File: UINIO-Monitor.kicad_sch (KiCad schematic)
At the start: 38 parts, among them J1 Conn_01x09_Male, J2 Conn_01x09_Male, J3 Conn_01x04_Male, P1 LCD_Pad_10Pin, P2 LCD_Pad_12Pin, P3 OLED_Pad_30Pin, U1 ME6211, U2 ME6211, U3 XC6206PxxxMR

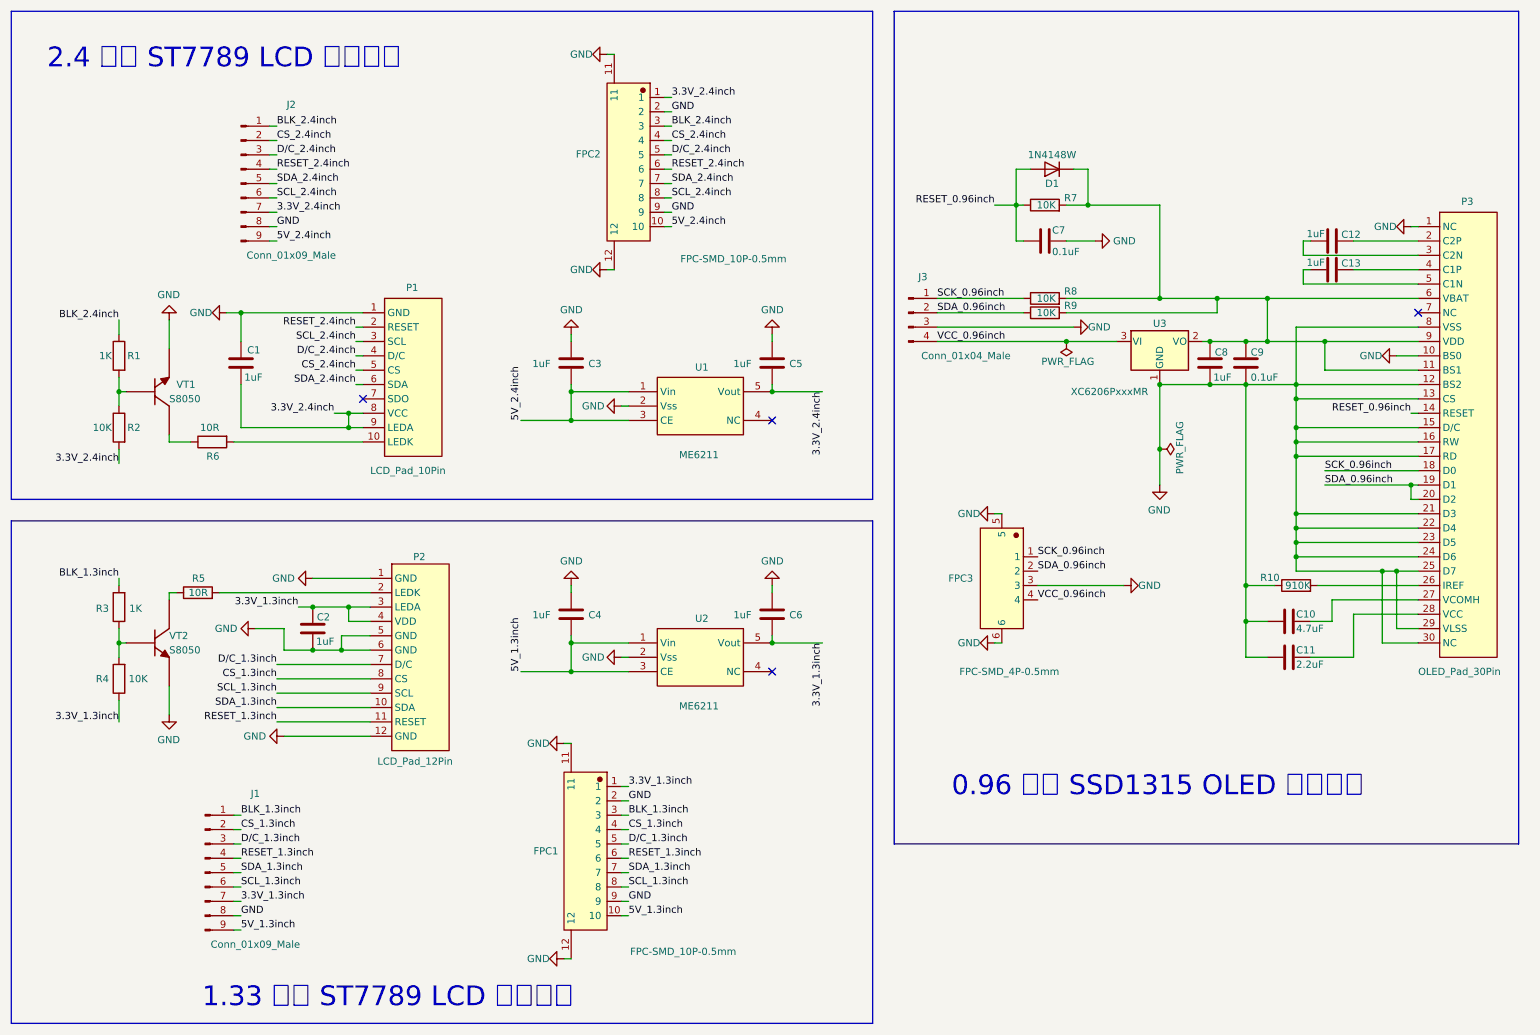
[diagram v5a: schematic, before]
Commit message: Complete PCB routing.
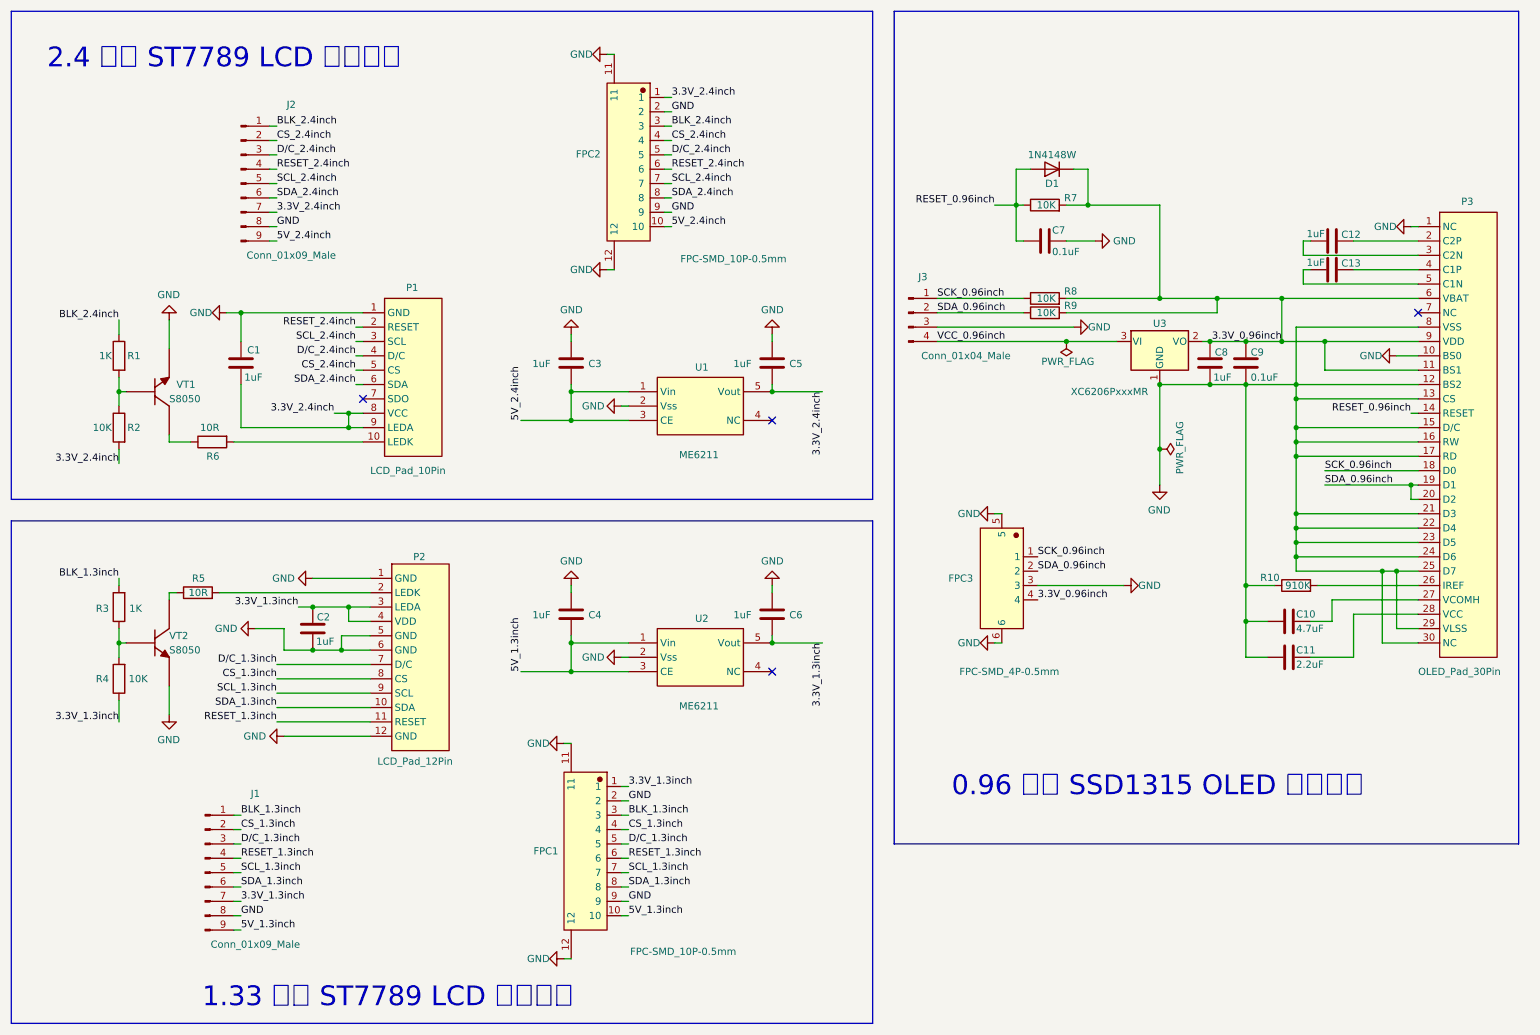
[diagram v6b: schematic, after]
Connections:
- net SCL_1.3inch: now also FPC1.7, J1.5 (Pin_5); no longer FPC1.8, J1.6 (Pin_6)
- net SCL_2.4inch: now also FPC2.7, J2.5 (Pin_5); no longer FPC2.8, J2.6 (Pin_6)
- net SDA_1.3inch: now also FPC1.8, J1.6 (Pin_6); no longer FPC1.7, J1.5 (Pin_5)
- net SDA_2.4inch: now also FPC2.8, J2.6 (Pin_6); no longer FPC2.7, J2.5 (Pin_5)
- net VCC_0.96inch: no longer FPC3.4
- net 3.3V_0.96inch: now reaches C8.2, C9.2, D1.1 (K), P3.11 (BS1), P3.6 (VBAT), P3.9 (VDD), R7.2, R8.2, R9.2, U3.2 (VO)
- net 3.3V_0.96inch: now also FPC3.4
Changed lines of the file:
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@@
   (junction (at 114.3 82.55) (diameter 0) (color 0 0 0 0)
   )
+  (junction (at 240.03 66.04) (diameter 0) (color 0 0 0 0)
+  )
   (junction (at 242.57 109.22) (diameter 0) (color 0 0 0 0)
   )
@@
   (junction (at 242.57 106.68) (diameter 0) (color 0 0 0 0)
   )
-  (junction (at 237.49 66.04) (diameter 0) (color 0 0 0 0)
-  )
   (junction (at 34.29 82.55) (diameter 0) (color 0 0 0 0)
   )
@@
   (junction (at 257.81 114.3) (diameter 0) (color 0 0 0 0)
   )
-  (junction (at 237.49 73.66) (diameter 0) (color 0 0 0 0)
-  )
   (junction (at 193.04 49.53) (diameter 0) (color 0 0 0 0)
   )
@@
   )
   (junction (at 242.57 93.98) (diameter 0) (color 0 0 0 0)
+  )
+  (junction (at 240.03 73.66) (diameter 0) (color 0 0 0 0)
   )
   (junction (at 218.44 81.28) (diameter 0) (color 0 0 0 0)
@@
     (stroke (width 0) (type default) (color 0 0 0 0))
   )
-  (wire (pts (xy 237.49 73.66) (xy 247.65 73.66))
-    (stroke (width 0) (type default) (color 0 0 0 0))
-  )
   (wire (pts (xy 201.93 68.58) (xy 228.6 68.58))
     (stroke (width 0) (type default) (color 0 0 0 0))
@@
     (stroke (width 0) (type default) (color 0 0 0 0))
   )
-  (wire (pts (xy 237.49 66.04) (xy 237.49 73.66))
+  (wire (pts (xy 240.03 66.04) (xy 240.03 73.66))
     (stroke (width 0) (type default) (color 0 0 0 0))
   )
@@
     (stroke (width 0) (type default) (color 0 0 0 0))
   )
-  (wire (pts (xy 228.6 66.04) (xy 237.49 66.04))
-    (stroke (width 0) (type default) (color 0 0 0 0))
-  )
   (wire (pts (xy 63.5 143.51) (xy 78.74 143.51))
     (stroke (width 0) (type default) (color 0 0 0 0))
@@
     (stroke (width 0) (type default) (color 0 0 0 0))
   )
+  (wire (pts (xy 240.03 73.66) (xy 247.65 73.66))
+    (stroke (width 0) (type default) (color 0 0 0 0))
+  )
   (wire (pts (xy 242.57 111.76) (xy 264.16 111.76))
     (stroke (width 0) (type default) (color 0 0 0 0))
@@
     (stroke (width 0) (type default) (color 0 0 0 0))
   )
+  (wire (pts (xy 240.03 66.04) (xy 264.16 66.04))
+    (stroke (width 0) (type default) (color 0 0 0 0))
+  )
   (wire (pts (xy 34.29 127) (xy 35.56 127))
     (stroke (width 0) (type default) (color 0 0 0 0))
@@
     (stroke (width 0) (type default) (color 0 0 0 0))
   )
-  (wire (pts (xy 237.49 66.04) (xy 264.16 66.04))
+  (wire (pts (xy 228.6 66.04) (xy 240.03 66.04))
     (stroke (width 0) (type default) (color 0 0 0 0))
   )
@@
     (stroke (width 0) (type default) (color 0 0 0 0))
   )
-  (wire (pts (xy 233.68 73.66) (xy 237.49 73.66))
+  (wire (pts (xy 233.68 73.66) (xy 240.03 73.66))
     (stroke (width 0) (type default) (color 0 0 0 0))
   )
@@
     (effects (font (size 1.27 1.27)) (justify right bottom))
   )
-  (label "SCL_1.3inch" (at 55.88 170.18 0)
-    (effects (font (size 1.27 1.27)) (justify left bottom))
-  )
-  (label "SDA_2.4inch" (at 62.23 45.72 0)
+  (label "SCL_1.3inch" (at 55.88 167.64 0)
+    (effects (font (size 1.27 1.27)) (justify left bottom))
+  )
+  (label "SDA_2.4inch" (at 62.23 48.26 0)
     (effects (font (size 1.27 1.27)) (justify left bottom))
   )
@@
     (effects (font (size 1.27 1.27)) (justify left bottom))
   )
-  (label "SDA_1.3inch" (at 124.46 167.64 0)
+  (label "SDA_1.3inch" (at 124.46 170.18 0)
     (effects (font (size 1.27 1.27)) (justify left bottom))
   )
@@
     (effects (font (size 1.27 1.27)) (justify left bottom))
   )
-  (label "SDA_2.4inch" (at 132.08 45.72 0)
+  (label "SDA_2.4inch" (at 132.08 48.26 0)
     (effects (font (size 1.27 1.27)) (justify left bottom))
   )
@@
     (effects (font (size 1.27 1.27)) (justify left bottom))
   )
-  (label "SCL_1.3inch" (at 124.46 170.18 0)
+  (label "SCL_1.3inch" (at 124.46 167.64 0)
     (effects (font (size 1.27 1.27)) (justify left bottom))
   )
@@
     (effects (font (size 1.27 1.27)) (justify right bottom))
   )
+  (label "3.3V_0.96inch" (at 240.03 73.66 180)
+    (effects (font (size 1.27 1.27)) (justify right bottom))
+  )
   (label "BLK_2.4inch" (at 62.23 35.56 0)
     (effects (font (size 1.27 1.27)) (justify left bottom))
@@
     (effects (font (size 1.27 1.27)) (justify left bottom))
   )
-  (label "SCL_2.4inch" (at 132.08 48.26 0)
+  (label "SCL_2.4inch" (at 132.08 45.72 0)
     (effects (font (size 1.27 1.27)) (justify left bottom))
   )
@@
     (effects (font (size 1.27 1.27)) (justify left bottom))
   )
-  (label "SDA_1.3inch" (at 55.88 167.64 0)
+  (label "SDA_1.3inch" (at 55.88 170.18 0)
     (effects (font (size 1.27 1.27)) (justify left bottom))
   )
@@
     (effects (font (size 1.27 1.27)) (justify right bottom))
   )
-  (label "SCL_2.4inch" (at 62.23 48.26 0)
+  (label "SCL_2.4inch" (at 62.23 45.72 0)
     (effects (font (size 1.27 1.27)) (justify left bottom))
   )
@@
     (effects (font (size 1.27 1.27)) (justify left bottom))
   )
-  (label "VCC_0.96inch" (at 196.85 119.38 0)
-    (effects (font (size 1.27 1.27)) (justify left bottom))
-  )
+  (label "3.3V_0.96inch" (at 196.85 119.38 0)
+    (effects (font (size 1.27 1.27)) (justify left bottom))
+  )

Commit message: Update PCB.
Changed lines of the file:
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@@
+    (stroke (width 0) (type default) (color 0 0 0 0))
+  )
+  (wire (pts (xy 238.76 104.14) (xy 242.57 104.14))
     (stroke (width 0) (type default) (color 0 0 0 0))
   )
@@
     (pin "1")
   )
+  (symbol (lib_id "power:GND") (at 238.76 104.14 270) (unit 1)
+    (in_bom yes) (on_board yes)
+    (property "Reference" "#PWR0101" (id 0) (at 232.41 104.14 0)
+      (effects (font (size 1.27 1.27)) hide)
+    )
+    (property "Value" "GND" (id 1) (at 238.76 101.6 90)
+      (effects (font (size 1.27 1.27)) (justify right))
+    )
+    (property "Footprint" "" (id 2) (at 238.76 104.14 0)
+      (effects (font (size 1.27 1.27)) hide)
+    )
+    (property "Datasheet" "" (id 3) (at 238.76 104.14 0)
+      (effects (font (size 1.27 1.27)) hide)
+    )
+    (pin "1")
+  )
   (symbol (lib_id "Device:C") (at 114.3 77.47 0) (unit 1)
     (in_bom yes) (on_board yes)
@@
       (reference "#PWR024") (unit 1) (value "GND") (footprint "")
     )
+    (path "/9499cd95-66cf-4b06-b6d6-0a8ce1698b2b"
+      (reference "#PWR0101") (unit 1) (value "GND") (footprint "")
+    )
     (path "/0efa37a5-698f-4007-a3bb-11fc0938c252"
